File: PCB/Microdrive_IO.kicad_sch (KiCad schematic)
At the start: 10 parts, among them Q9 BC184C

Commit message: feat: Upload initial PCB v0.3
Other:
- title: ZXTeensyIF1 -> ${PRJ_NAME}
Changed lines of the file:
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@@
 	(paper "A4")
 	(title_block
-		(title "ZXTeensyIF1")
-		(date "2026-01-04")
-		(rev "0.1")
+		(title "${PRJ_NAME}")
+		(date "${PRJ_DATE}")
+		(rev "${PRJ_REVISION}")
 	)
 	(junction

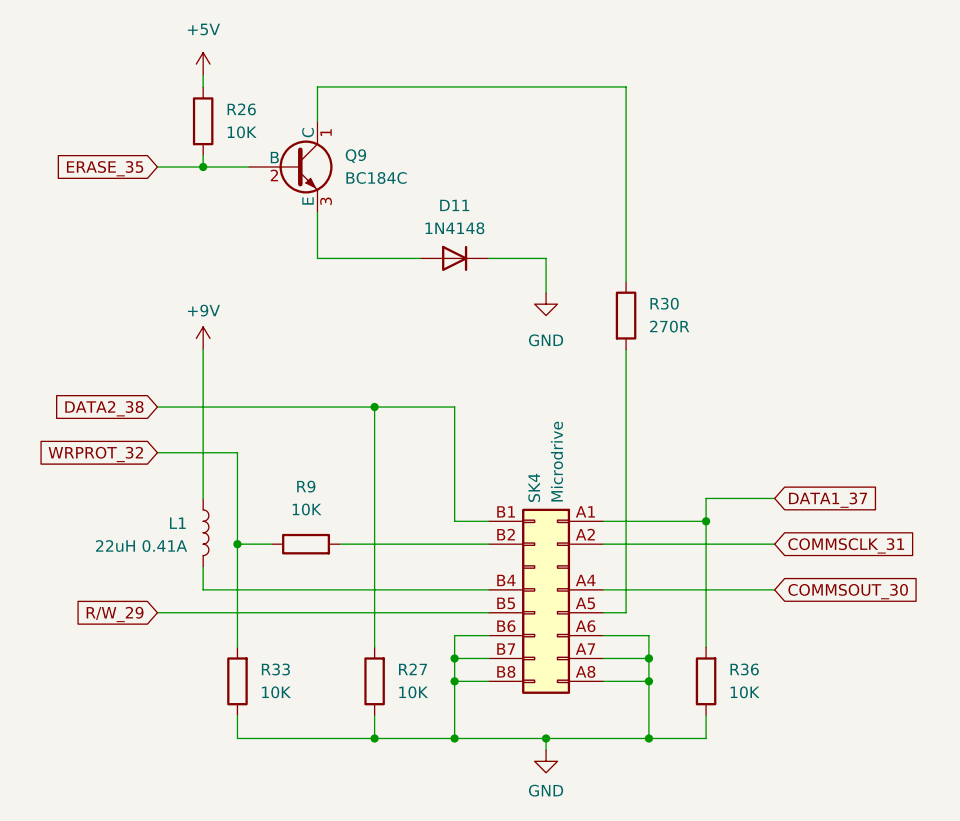
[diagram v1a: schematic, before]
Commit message: feat: Add ESP-01S header to PCB v0.5
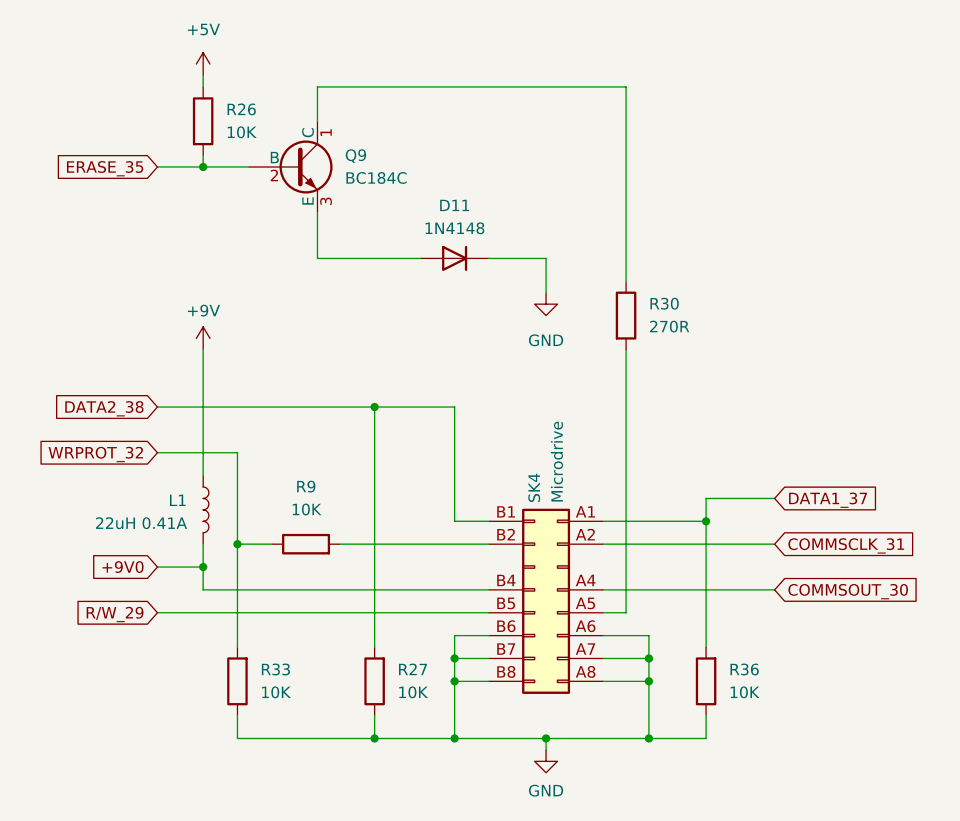
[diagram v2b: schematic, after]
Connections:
- net +9V0: now reaches L1.2, SK4.B4 (Pin_B4)
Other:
- moved on the sheet: L1
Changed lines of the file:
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@@
+	)
+	(junction
+		(at 68.58 85.09)
+		(diameter 0)
+		(color 0 0 0 0)
 	)
 	(junction
@@
 	(wire
 		(pts
+			(xy 73.66 40.64) (xy 68.58 40.64)
+		)
+		(stroke
+			(width 0)
+			(type default)
+		)
+	)
+	(wire
+		(pts
+			(xy 106.68 105.41) (xy 106.68 104.14)
+		)
+		(stroke
+			(width 0)
+			(type default)
+		)
+	)
+	(wire
+		(pts
+			(xy 72.39 104.14) (xy 87.63 104.14)
+		)
+		(stroke
+			(width 0)
+			(type default)
+		)
+	)
+	(wire
+		(pts
+			(xy 132.08 87.63) (xy 113.03 87.63)
+		)
+		(stroke
+			(width 0)
+			(type default)
+		)
+	)
+	(wire
+		(pts
+			(xy 87.63 101.6) (xy 87.63 104.14)
+		)
+		(stroke
+			(width 0)
+			(type default)
+		)
+	)
+	(wire
+		(pts
+			(xy 113.03 95.25) (xy 118.11 95.25)
+		)
+		(stroke
+			(width 0)
+			(type default)
+		)
+	)
+	(wire
+		(pts
+			(xy 68.58 60.96) (xy 68.58 74.93)
+		)
+		(stroke
+			(width 0)
+			(type default)
+		)
+	)
+	(wire
+		(pts
+			(xy 118.11 97.79) (xy 118.11 104.14)
+		)
+		(stroke
+			(width 0)
+			(type default)
+		)
+	)
+	(wire
+		(pts
+			(xy 96.52 80.01) (xy 100.33 80.01)
+		)
+		(stroke
+			(width 0)
+			(type default)
+		)
+	)
+	(wire
+		(pts
 			(xy 68.58 85.09) (xy 68.58 87.63)
 		)
@@
 	(wire
 		(pts
-			(xy 73.66 40.64) (xy 68.58 40.64)
-		)
-		(stroke
-			(width 0)
-			(type default)
-		)
-	)
-	(wire
-		(pts
-			(xy 106.68 105.41) (xy 106.68 104.14)
-		)
-		(stroke
-			(width 0)
-			(type default)
-		)
-	)
-	(wire
-		(pts
-			(xy 72.39 104.14) (xy 87.63 104.14)
-		)
-		(stroke
-			(width 0)
-			(type default)
-		)
-	)
-	(wire
-		(pts
-			(xy 132.08 87.63) (xy 113.03 87.63)
-		)
-		(stroke
-			(width 0)
-			(type default)
-		)
-	)
-	(wire
-		(pts
-			(xy 87.63 101.6) (xy 87.63 104.14)
-		)
-		(stroke
-			(width 0)
-			(type default)
-		)
-	)
-	(wire
-		(pts
-			(xy 113.03 95.25) (xy 118.11 95.25)
-		)
-		(stroke
-			(width 0)
-			(type default)
-		)
-	)
-	(wire
-		(pts
-			(xy 68.58 60.96) (xy 68.58 77.47)
-		)
-		(stroke
-			(width 0)
-			(type default)
-		)
-	)
-	(wire
-		(pts
-			(xy 118.11 97.79) (xy 118.11 104.14)
-		)
-		(stroke
-			(width 0)
-			(type default)
-		)
-	)
-	(wire
-		(pts
-			(xy 96.52 80.01) (xy 100.33 80.01)
-		)
-		(stroke
-			(width 0)
-			(type default)
-		)
-	)
-	(wire
-		(pts
 			(xy 118.11 95.25) (xy 118.11 97.79)
 		)
@@
 	(wire
 		(pts
+			(xy 68.58 82.55) (xy 68.58 85.09)
+		)
+		(stroke
+			(width 0)
+			(type default)
+		)
+	)
+	(wire
+		(pts
 			(xy 96.52 95.25) (xy 100.33 95.25)
 		)
@@
 	(wire
 		(pts
-			(xy 100.33 87.63) (xy 68.58 87.63)
+			(xy 68.58 87.63) (xy 100.33 87.63)
+		)
+		(stroke
+			(width 0)
+			(type default)
+		)
+	)
+	(wire
+		(pts
+			(xy 68.58 85.09) (xy 63.5 85.09)
 		)
 		(stroke
@@
 				)
 				(justify left)
+			)
+		)
+	)
+	(global_label "+9V0"
+		(shape input)
+		(at 63.5 85.09 180)
+		(fields_autoplaced yes)
+		(effects
+			(font
+				(size 1.27 1.27)
+			)
+			(justify right)
+		)
+		(property "Intersheetrefs" "${INTERSHEET_REFS}"
+			(at 55.4348 85.09 0)
+			(effects
+				(font
+					(size 1.27 1.27)
+				)
+				(justify right)
 			)
 		)
@@
 	(symbol
 		(lib_id "Device:L")
-		(at 68.58 81.28 0)
+		(at 68.58 78.74 0)
 		(unit 1)
 		(exclude_from_sim no)
@@
 		(dnp no)
 		(property "Reference" "L1"
+			(at 66.802 77.724 0)
+			(effects
+				(font
+					(size 1.27 1.27)
+				)
+				(justify right)
+			)
+		)
+		(property "Value" "22uH 0.41A"
 			(at 66.802 80.264 0)
 			(effects
@@
 			)
 		)
-		(property "Value" "22uH 0.41A"
-			(at 66.802 82.804 0)
-			(effects
-				(font
-					(size 1.27 1.27)
-				)
-				(justify right)
-			)
-		)
 		(property "Footprint" "Inductor_THT:L_Axial_L12.8mm_D5.8mm_P20.32mm_Horizontal_Fastron_HBCC"
-			(at 68.58 81.28 0)
+			(at 68.58 78.74 0)
 			(effects
 				(font
@@
 		)
 		(property "Datasheet" "~"
-			(at 68.58 81.28 0)
+			(at 68.58 78.74 0)
 			(effects
 				(font
@@
 		)
 		(property "Description" ""
-			(at 68.58 81.28 0)
-			(effects
-				(font
+			(at 68.58 78.74 0)
+			(effects
+				(font
